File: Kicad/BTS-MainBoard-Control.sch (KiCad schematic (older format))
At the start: 26 parts, among them J3 Input Signals Connector, J4 Out connector, Q1 DMG3418L-7, U1 HIP4080A

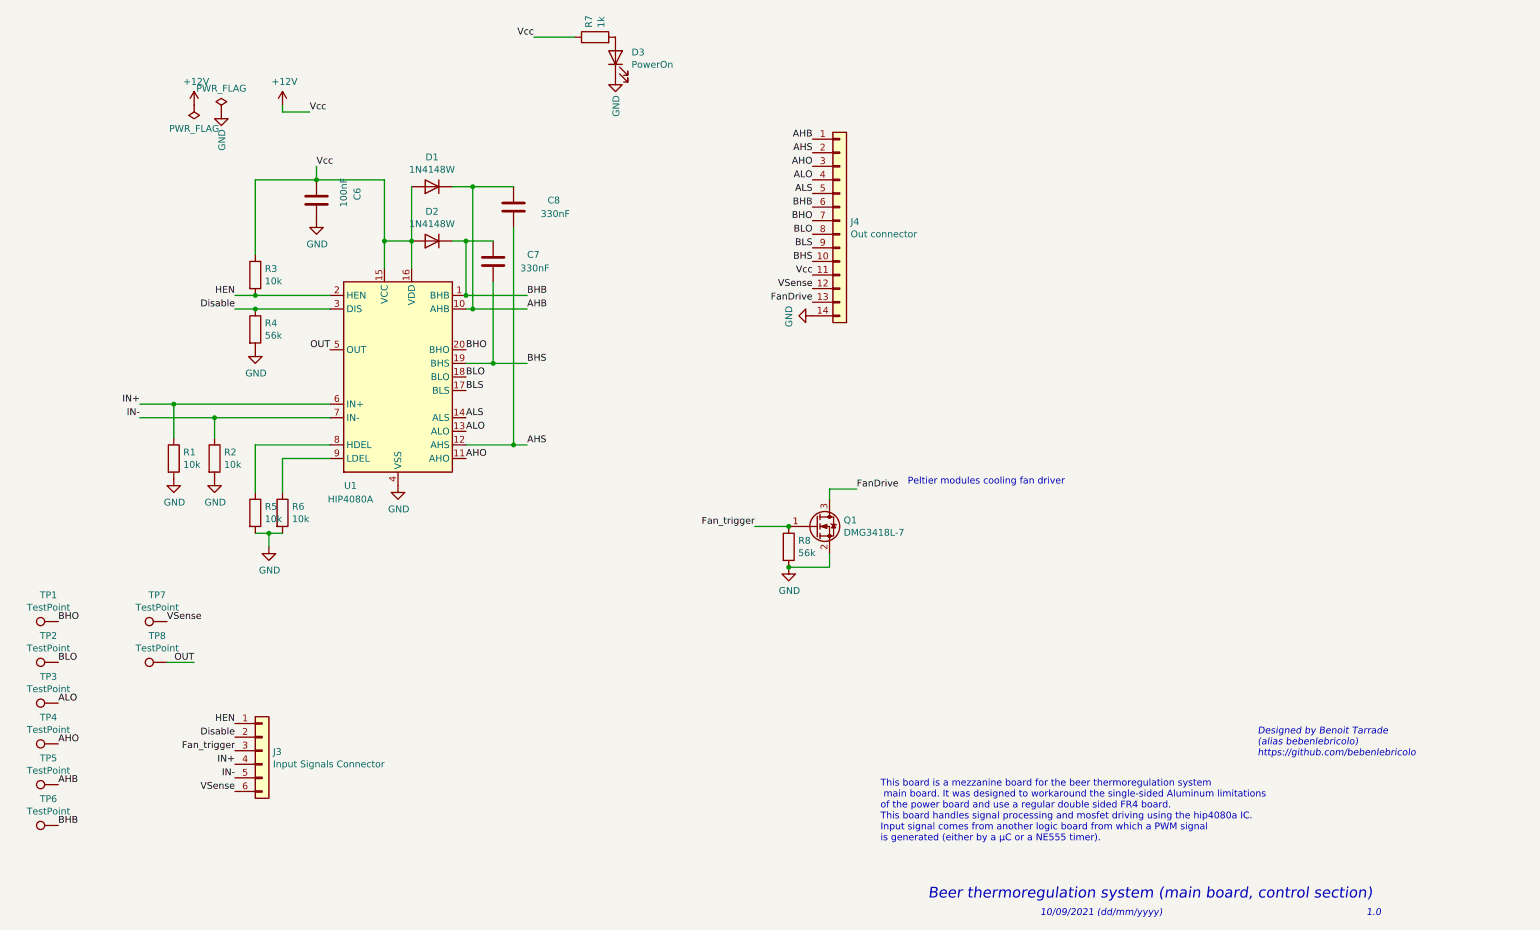
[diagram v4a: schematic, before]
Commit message: Updated the board to Revsision 1.1 : changed driver ICs
Signed-off-by: bebenlebricolo <benoittarrade@hotmail.fr>
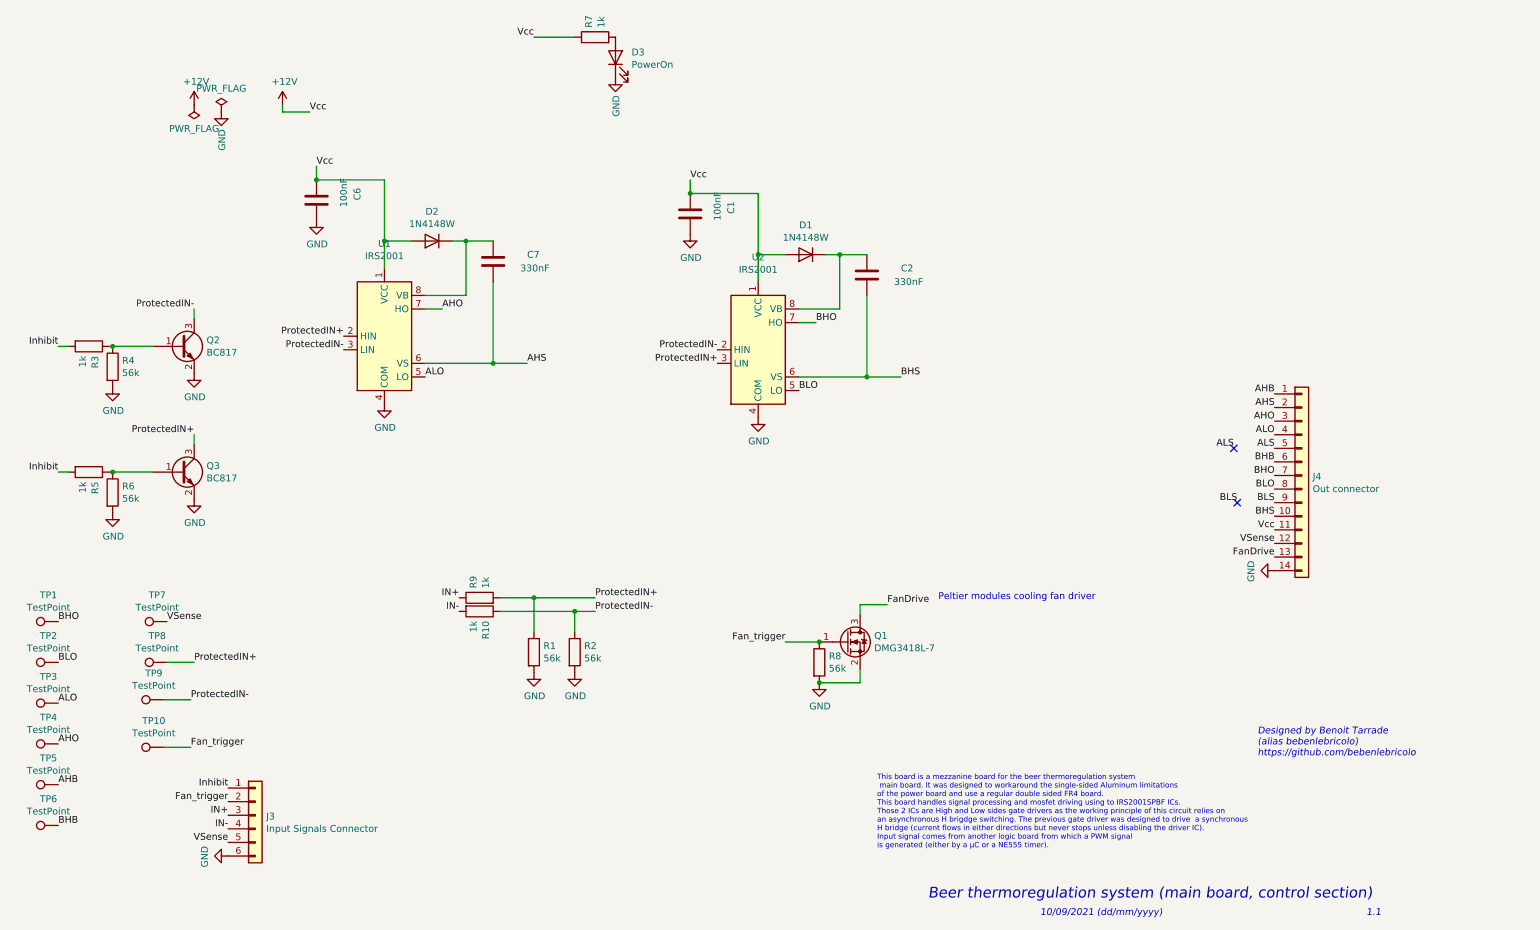
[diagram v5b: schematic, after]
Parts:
- removed C8: 330nF, Capacitor_SMD:C_1206_3216Metric_Pad1.33x1.80mm_HandSolder, symbol Device:C
- removed U1: HIP4080A, Package_SO:SOIC-20W_7.5x12.8mm_P1.27mm, symbol Driver_FET:HIP4080A
- added C1: 100nF, Capacitor_SMD:C_1206_3216Metric_Pad1.33x1.80mm_HandSolder, symbol Device:C
- added C2: 330nF, Capacitor_SMD:C_1206_3216Metric_Pad1.33x1.80mm_HandSolder, symbol Device:C
- added Q2, Q3: BC817, Package_TO_SOT_SMD:SOT-23, symbol Transistor_BJT:BC817
- added R10, R9: 1k, Resistor_SMD:R_1206_3216Metric_Pad1.30x1.75mm_HandSolder, symbol Device:R
- added TP10, TP9: TestPoint, TestPoint:TestPoint_Pad_D1.0mm, symbol Connector:TestPoint
- added U1, U2: IRS2001, Package_SO:SOIC-8_3.9x4.9mm_P1.27mm, symbol Driver_FET:IRS2001
- R1, R2, R6: value 10k -> 56k
- R3, R5: value 10k -> 1k
- TP1, TP2, TP3, TP4, TP5, TP6, TP7, TP8: footprint TestPoint:TestPoint_Pad_D2.0mm -> TestPoint:TestPoint_Pad_D1.0mm
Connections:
- net +12V: now also C1.1, U1.1 (VCC), U2.1 (VCC); no longer R3.1
- net AHB: no longer D1.1 (K)
- net AHO: now also U1.7 (HO)
- net AHS: now also C7.2, U1.6 (VS)
- net ALO: now also U1.5 (LO)
- net BHB: no longer C7.1, D2.1 (K)
- net BHO: now also U2.7 (HO)
- net BHS: now also C2.2, U2.6 (VS); no longer C7.2
- net BLO: now also U2.5 (LO)
- net Fan_trigger: now also J3.2 (Pin_2), TP10.1; no longer J3.3 (Pin_3)
- net GND: now also J3.6 (Pin_6), C1.2, Q2.2 (E), Q3.2 (E), U1.4 (COM), U2.4 (COM); no longer R5.2
- net IN+: now also J3.3 (Pin_3), R9.1; no longer J3.4 (Pin_4), R1.1
- net IN-: now also J3.4 (Pin_4), R10.2; no longer J3.5 (Pin_5), R2.1
- net VSense: now also J3.5 (Pin_5); no longer J3.6 (Pin_6)
- net at R5.1: now also R6.1, Q3.1 (B)
- net Disable: no longer names the net of R4.1
- net Disable: now also R3.1, Q2.1 (B); no longer J3.2 (Pin_2)
- net HEN renamed Inhibit
- net Inhibit: now also R5.2
- net OUT renamed ProtectedIN+
- net ProtectedIN+: now also R1.1, Q3.3 (C), R9.2, U1.2 (HIN), U2.3 (LIN)
- new net: C7.1, D2.1 (K), U1.8 (VB)
- new net: C2.1, D1.1 (K), U2.8 (VB)
- new net ProtectedIN-: Q2.3 (C), R10.1, R2.1, TP9.1, U1.3 (LIN), U2.2 (HIN)
- no-connect marks 0 -> 2
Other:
- note added: "1.1"
- note added: "This board is a mezzanine board for the beer thermoregulation system\n main board. It was designed to workaround the single-sided Aluminum limitations\nof the power board and use a regular double sided FR4 board.\nThis board handles signal processing and mosfet driving using to IRS2001SPBF ICs.\nThose 2 ICs are High and Low sides gate drivers as the working principle of this circuit relies on \na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"
- note removed: "1.0"
- note removed: "This board is a mezzanine board for the beer thermoregulation system\n main board. It was designed to workaround the single-sided Aluminum limitations\nof the power board and use a regular double sided FR4 board.\nThis board handles signal processing and mosfet driving using the hip4080a IC.\nInput signal comes from another logic board from which a PWM signal \nis generated (either by a µC or a N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"
- moved on the sheet: J3, J4, Q1, R1, R2, R4, R8
